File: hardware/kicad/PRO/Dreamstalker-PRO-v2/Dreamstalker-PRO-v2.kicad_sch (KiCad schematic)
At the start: 109 parts, among them J1 UART Header, J2 JTAG Header, J3 ST-033, J4 ATTEND_112J-TDAR-R01, J5 USB Power, J6 Li-Po 3.7V, M1 Vibration Motor, Q1 IRLML2402, Q2 BC807-40, Q3 BC807-40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

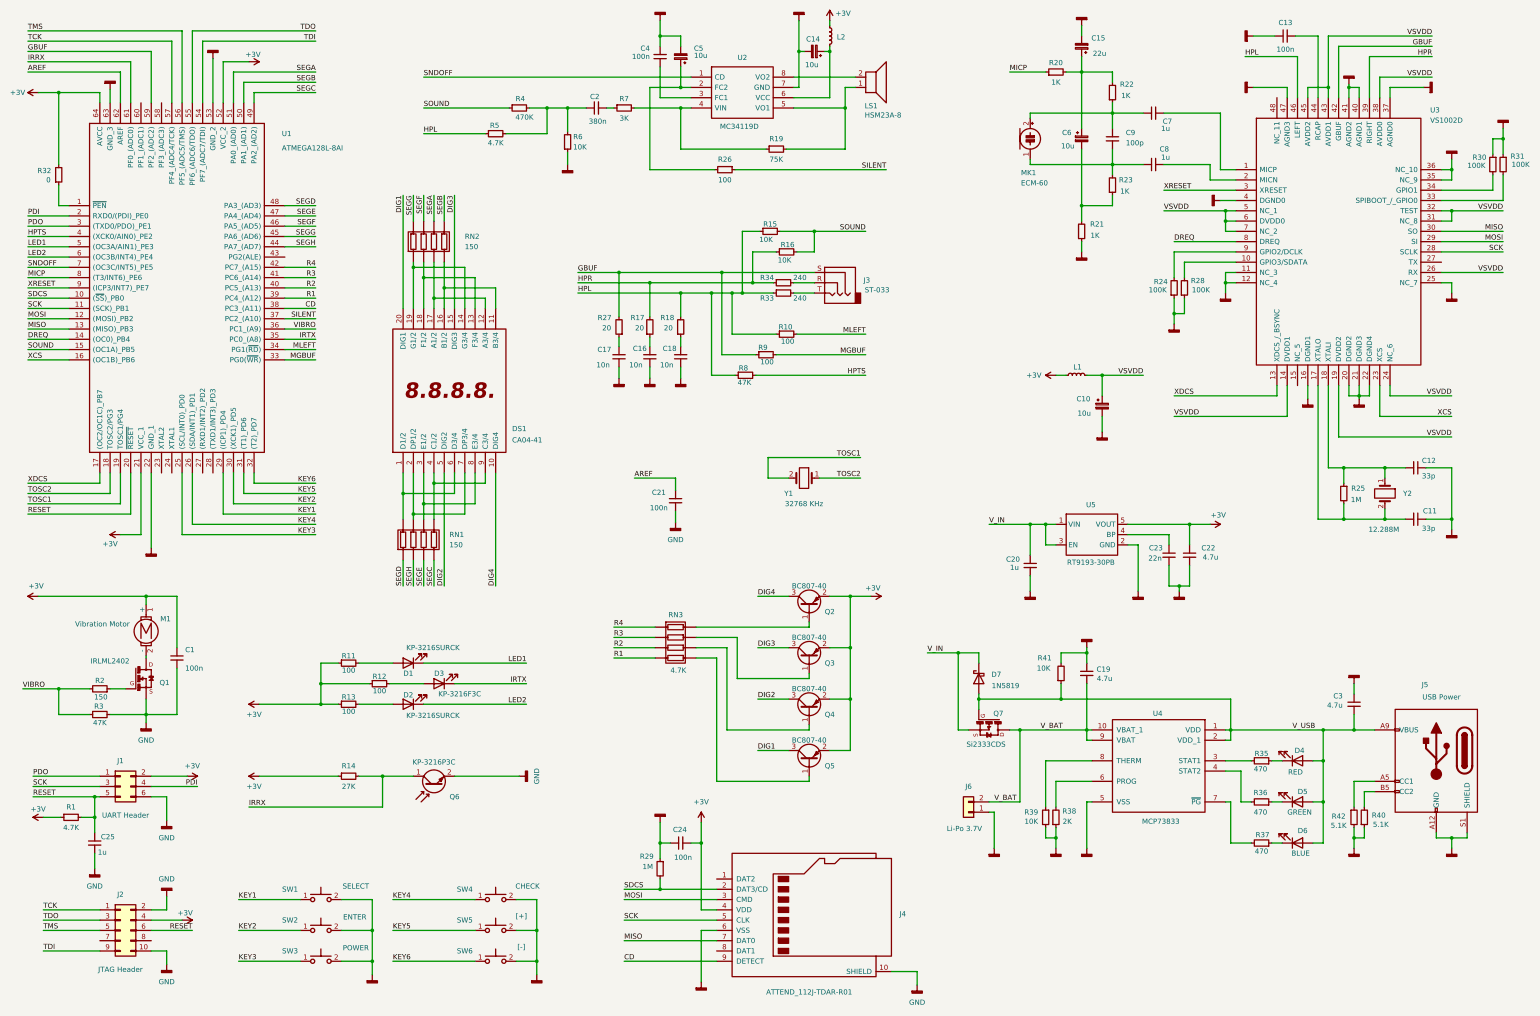
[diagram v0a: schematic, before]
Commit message: 1) Fixed: battery monitor not able to detect low-battery state (Now get battery monitor signal from LDO input). 2) Other planned updates.
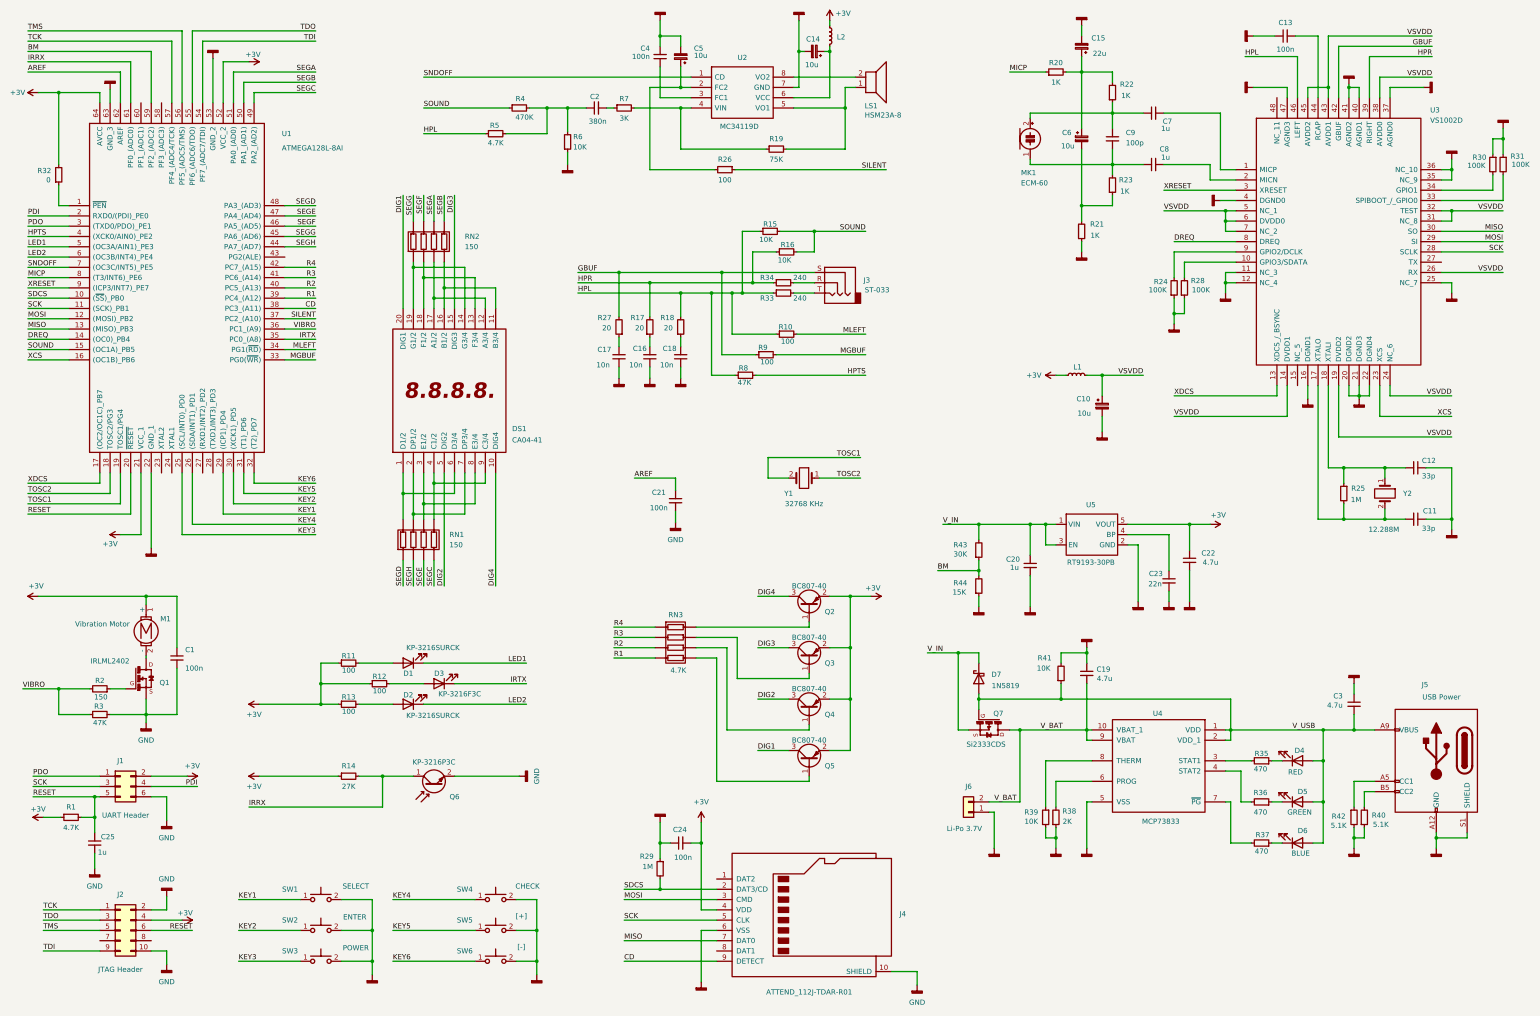
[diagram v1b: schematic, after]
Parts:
- added R43: 30K, Dreamstalker-Footprints:R_0603_1608Metric, symbol Dreamstalker-Components:R_Small
- added R44: 15K, Dreamstalker-Footprints:R_0603_1608Metric, symbol Dreamstalker-Components:R_Small
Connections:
- net GBUF: no longer U1.59 (PF2_(ADC2))
- net GND: now also R44.1
- net V_IN: now also R43.2
- new net BM: R43.1, R44.2, U1.59 (PF2_(ADC2))
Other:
- moved on the sheet: C22, C23

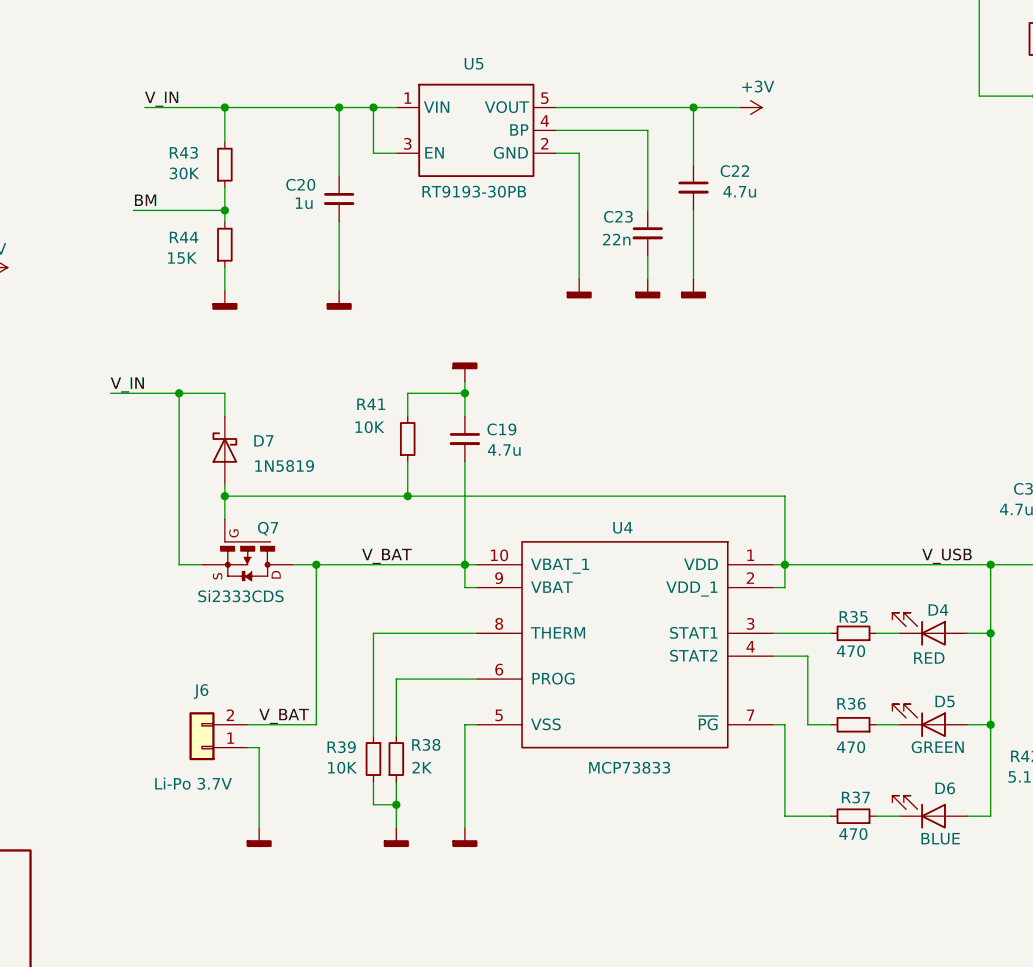
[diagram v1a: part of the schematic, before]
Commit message: New REM detect algorithm; New visualization in qtdreamflowmanager; Lots of bugfix
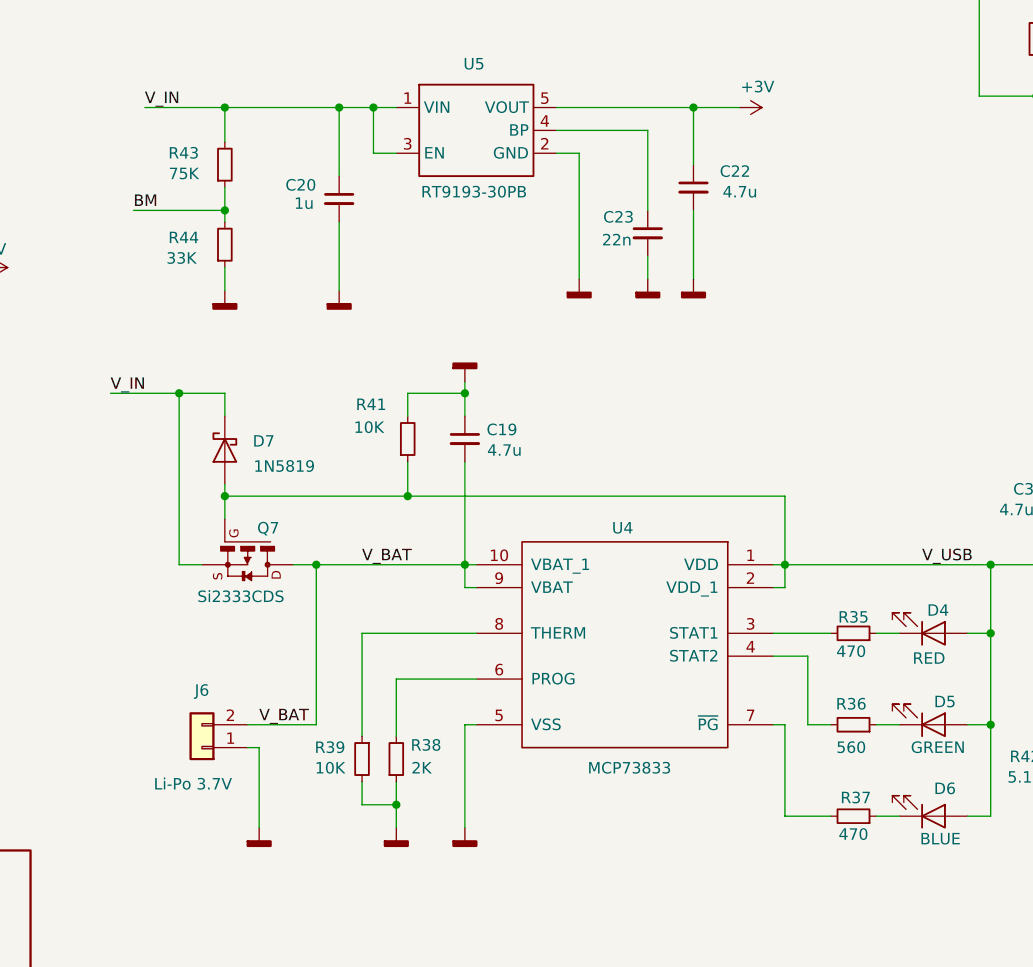
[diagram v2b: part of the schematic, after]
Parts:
- R36: value 470 -> 560
- R43: value 30K -> 75K
- R44: value 15K -> 33K
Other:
- moved on the sheet: R39
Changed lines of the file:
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@@
 	(wire
 		(pts
-			(xy 280.67 231.14) (xy 283.21 231.14)
+			(xy 279.4 231.14) (xy 283.21 231.14)
 		)
 		(stroke
@@
 	(wire
 		(pts
-			(xy 280.67 212.09) (xy 280.67 223.52)
+			(xy 279.4 212.09) (xy 279.4 223.52)
 		)
 		(stroke
@@
 	(wire
 		(pts
-			(xy 280.67 212.09) (xy 292.1 212.09)
+			(xy 279.4 212.09) (xy 292.1 212.09)
 		)
 		(stroke
@@
 	(wire
 		(pts
-			(xy 280.67 228.6) (xy 280.67 231.14)
+			(xy 279.4 228.6) (xy 279.4 231.14)
 		)
 		(stroke
@@
 			)
 		)
-		(property "Value" "15K"
+		(property "Value" "33K"
 			(at 259.334 170.434 0)
 			(effects
@@
 			)
 		)
-		(property "Value" "30K"
+		(property "Value" "75K"
 			(at 259.588 161.036 0)
 			(effects
@@
 		(lib_name "R_Small_1")
 		(lib_id "Dreamstalker-Components:R_Small")
-		(at 280.67 226.06 0)
+		(at 279.4 226.06 0)
 		(mirror y)
 		(unit 1)
@@
 		(dnp no)
 		(property "Reference" "R39"
-			(at 277.114 224.79 0)
+			(at 275.844 224.79 0)
 			(effects
 				(font
@@
 		)
 		(property "Value" "10K"
-			(at 277.114 227.076 0)
+			(at 275.844 227.076 0)
 			(effects
 				(font
@@
 		)
 		(property "Footprint" "Dreamstalker-Footprints:R_0603_1608Metric"
-			(at 280.67 226.06 0)
+			(at 279.4 226.06 0)
 			(effects
 				(font
@@
 		)
 		(property "Datasheet" "~"
-			(at 280.67 226.06 0)
+			(at 279.4 226.06 0)
 			(effects
 				(font
@@
 		)
 		(property "Description" "Resistor, small symbol"
-			(at 280.67 226.06 0)
+			(at 279.4 226.06 0)
 			(effects
 				(font
@@
 			)
 		)
-		(property "Value" "470"
+		(property "Value" "560"
 			(at 333.756 224.79 90)
 			(effects
